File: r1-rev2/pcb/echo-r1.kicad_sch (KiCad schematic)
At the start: 82 parts, among them J2 TYPE-C-31-M-12, J3 TF-115, J6 PM254-1-06-W-8.5, J7 ILI9342C, J8 Conn_01x04, Q4 AO3401A, SW1 POWER, SW10 DPAD→, SW11 START, SW12 SELECT, SW13 VOL+, SW14 VOL-, SW2 HOLD, SW3 A, SW4 B, SW5 X, SW6 Y, SW7 DPAD↑, SW8 DPAD↓, SW9 DPAD←, U7 STM32H7R3Z8Jx, U8 W958D8NBYA5I, Y1 SC-32S32.768kHz20PPM12.5pF, Y2 XTM32024000JT00351001

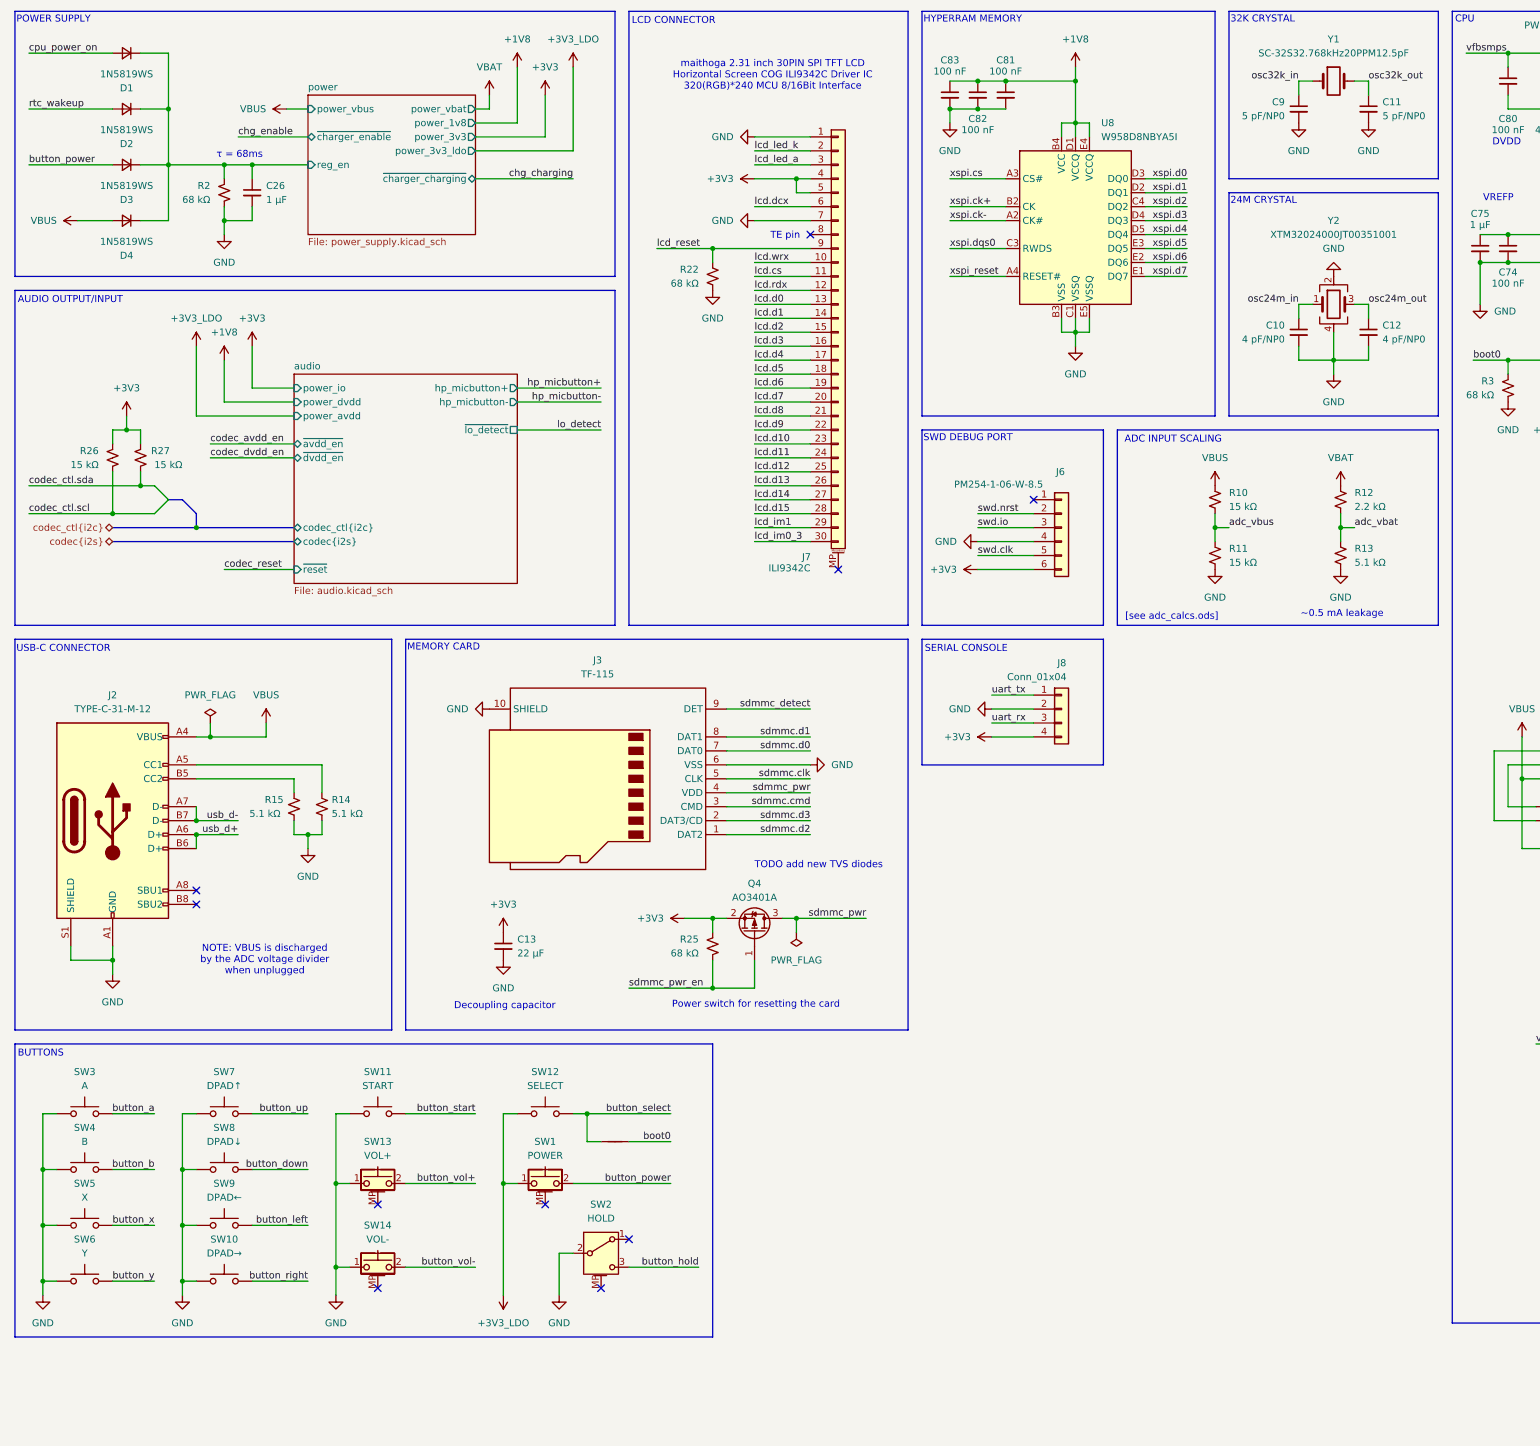
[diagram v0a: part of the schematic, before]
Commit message: R1-Rev2: add TVS diodes to external connectors
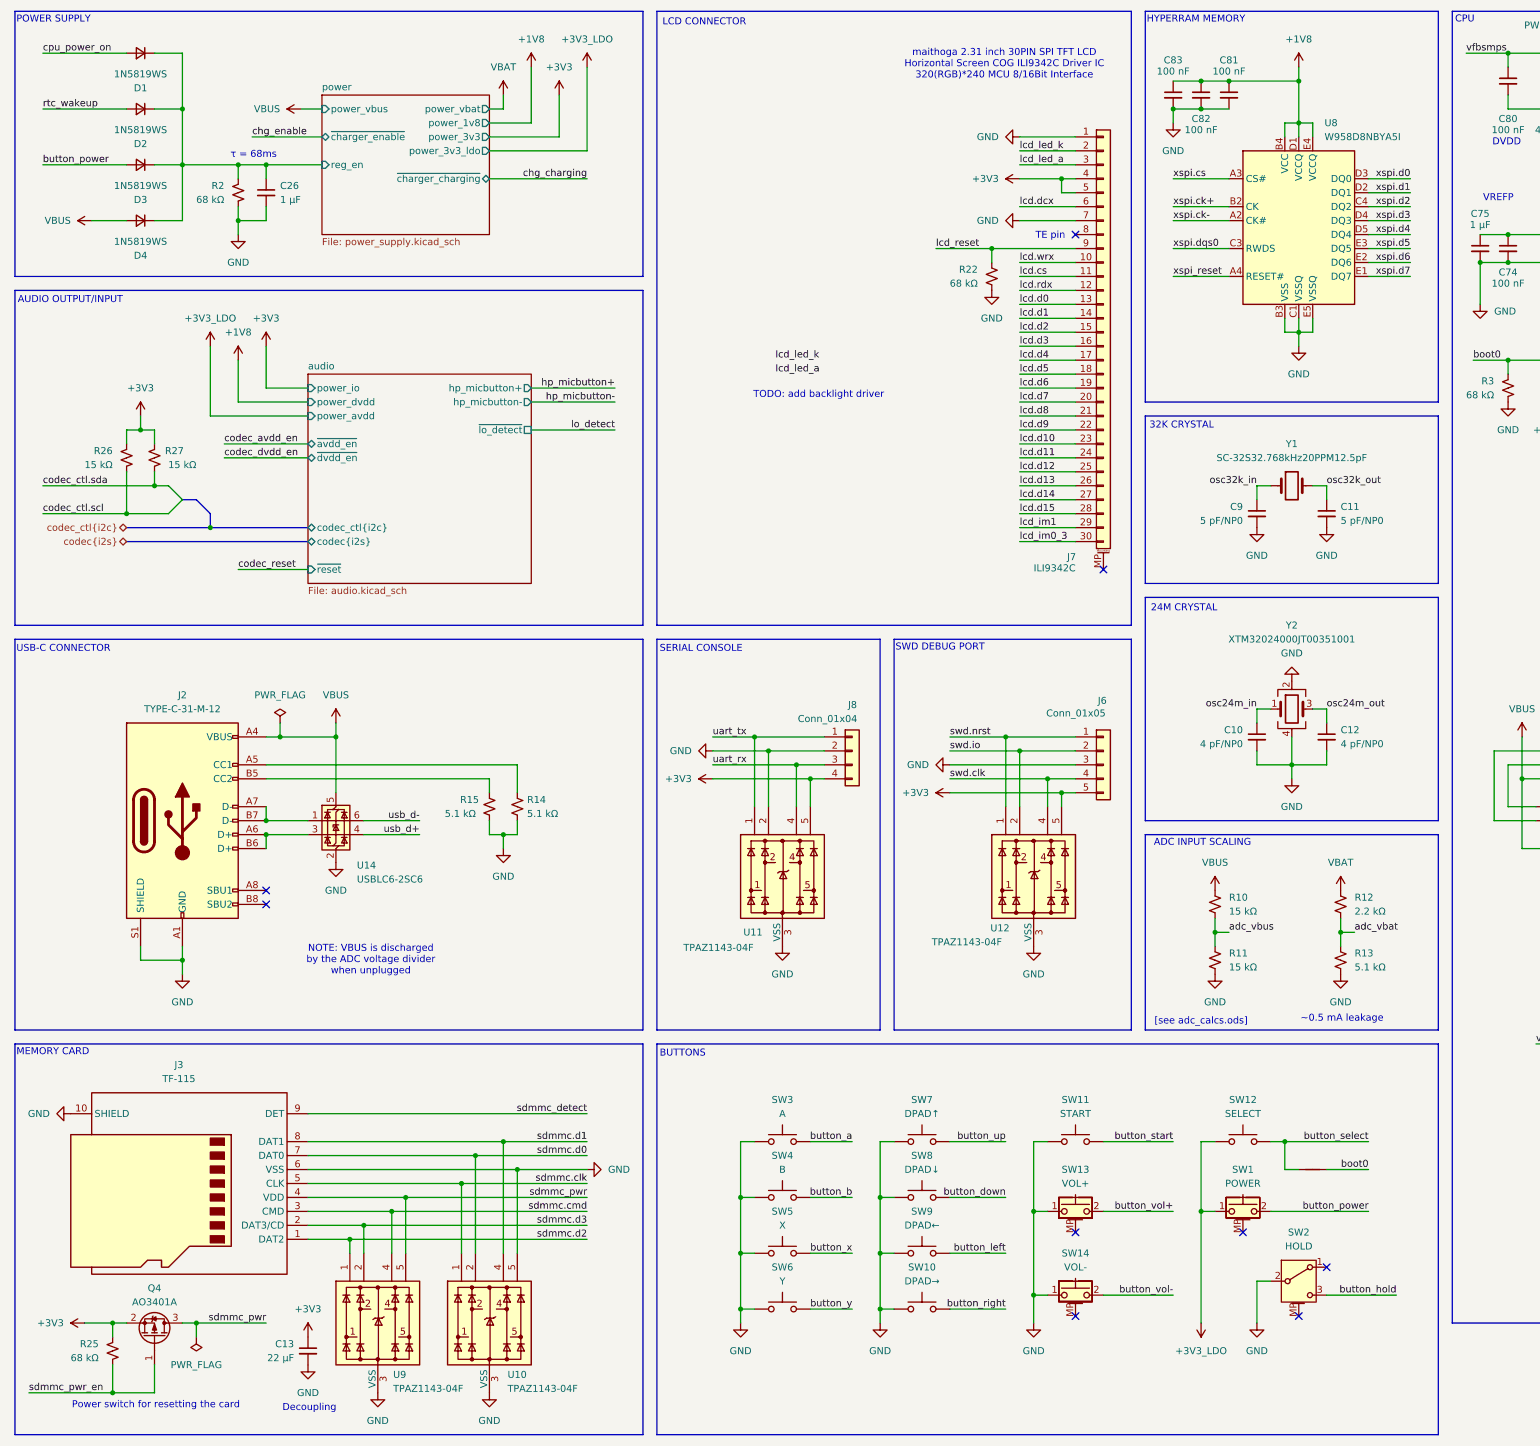
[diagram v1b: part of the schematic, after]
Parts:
- removed J6: PM254-1-06-W-8.5, Connector_PinSocket_2.54mm:PinSocket_1x06_P2.54mm_Horizontal, symbol Connector_Generic:Conn_01x06
- added J6: Conn_01x05, symbol Connector_Generic:Conn_01x05
- added U10, U11, U12, U9: TPAZ1143-04F, echoplayer:TECHPUBLIC_UDFN-10_1.0x2.5mm_P0.5mm, symbol echoplayer:TPAZ1143-04F
- added U14: USBLC6-2SC6, Package_TO_SOT_SMD:SOT-23-6, symbol Power_Protection:USBLC6-2SC6
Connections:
- net +3V3: now also J6.5 (Pin_5), U11.5, U12.5
- net GND: now also J6.3 (Pin_3), U10.10 (NC), U10.3 (VSS), U10.5, U10.6 (NC), U10.7 (NC), U10.8 (VSS), U10.9 (NC), U11.10 (NC), U11.2, U11.3 (VSS), U11.6 (NC), U11.7 (NC), U11.8 (VSS), U11.9 (NC), U12.10 (NC), U12.3 (VSS), U12.6 (NC), U12.7 (NC), U12.8 (VSS), U12.9 (NC), U14.2 (GND), U9.10 (NC), U9.3 (VSS), U9.6 (NC), U9.7 (NC), U9.8 (VSS), U9.9 (NC)
- net VBUS: now also U14.5 (VBUS)
- net sdmmc.clk: now also U10.1
- net sdmmc.cmd: now also U9.4
- net sdmmc.d0: now also U10.2
- net sdmmc.d1: now also U10.4
- net sdmmc.d2: now also U9.1
- net sdmmc.d3: now also U9.2
- net sdmmc_pwr: now also U9.5
- net swd.clk: now also J6.4 (Pin_4), U12.4
- net swd.io: now also J6.2 (Pin_2), U12.2
- net swd.nrst: now also J6.1 (Pin_1), U12.1
- net uart_rx: now also U11.4
- net uart_tx: now also U11.1
- net usb_d+: now also U14.4 (I/O2); no longer J2.A6 (D+), J2.B6 (D+)
- net usb_d-: now also U14.6 (I/O1); no longer J2.A7 (D-), J2.B7 (D-)
- new net: J2.A7 (D-), J2.B7 (D-), U14.1 (I/O1)
- new net: J2.A6 (D+), J2.B6 (D+), U14.3 (I/O2)
- no-connect marks 12 -> 11
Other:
- note added: "Decoupling"
- note added: "TODO: add backlight driver"
- note removed: "Decoupling capacitor"
- note removed: "TODO add new TVS diodes"
- moved on the sheet: C10, C11, C12, C13, C26, C81, C82, C83, C9, D1, D2, D3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

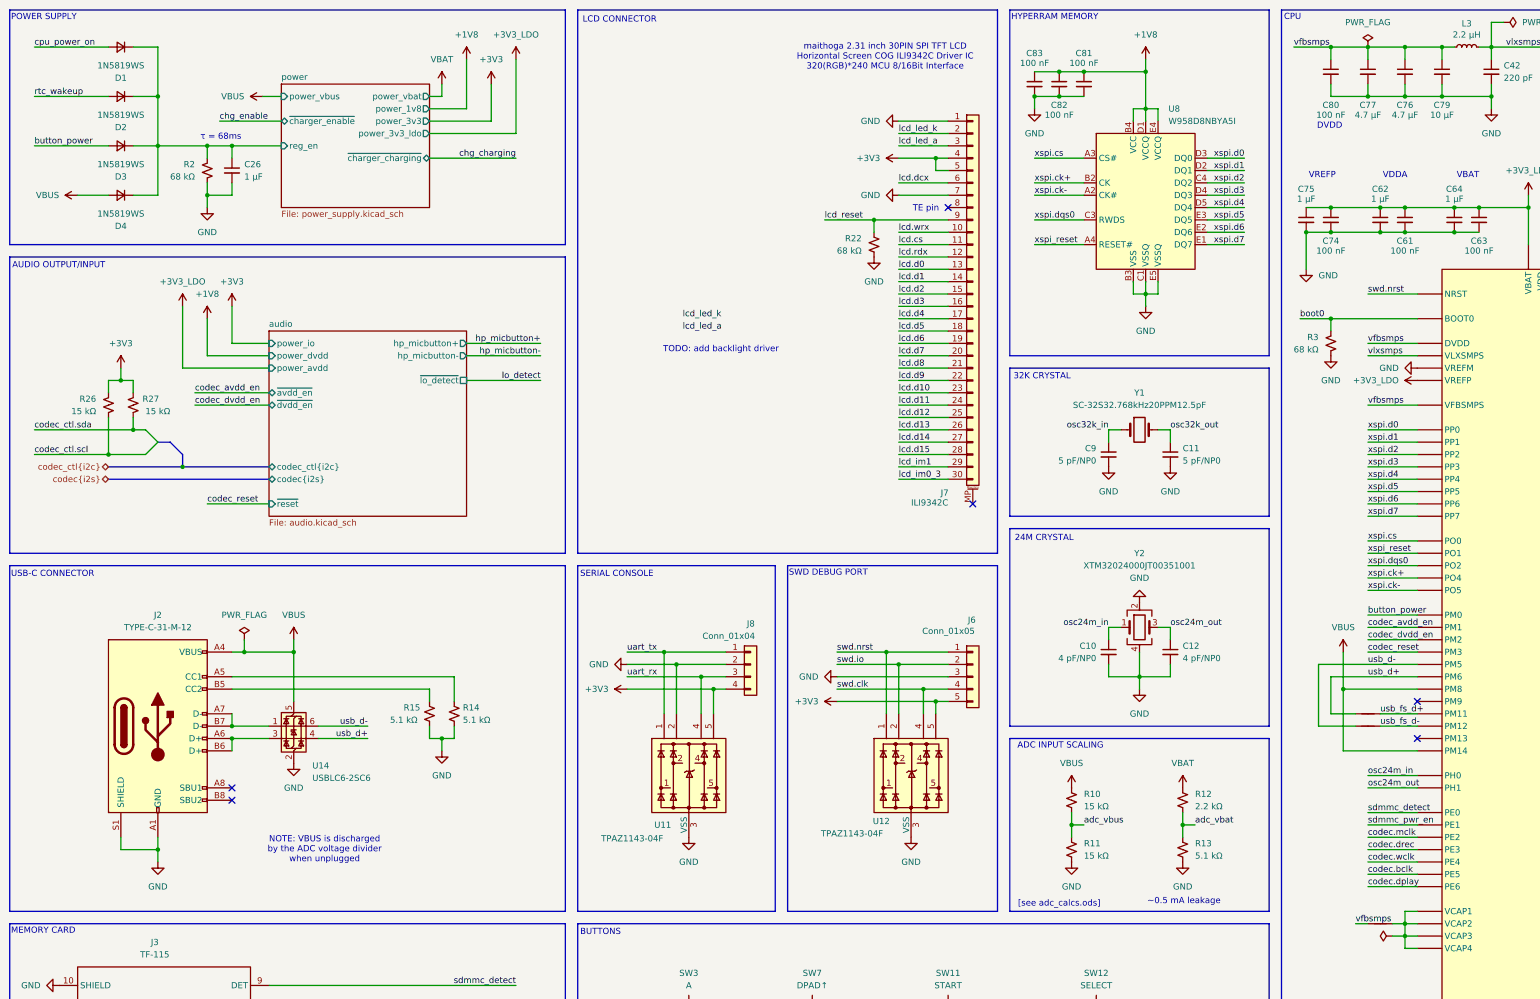
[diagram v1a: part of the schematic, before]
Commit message: R1-Rev2: add LCD backlight driver
The LEDs in the backlight will be in series since there are only
two pins, but it's not clear how many LEDs are there and without
that it's not possible to set the right current limit.
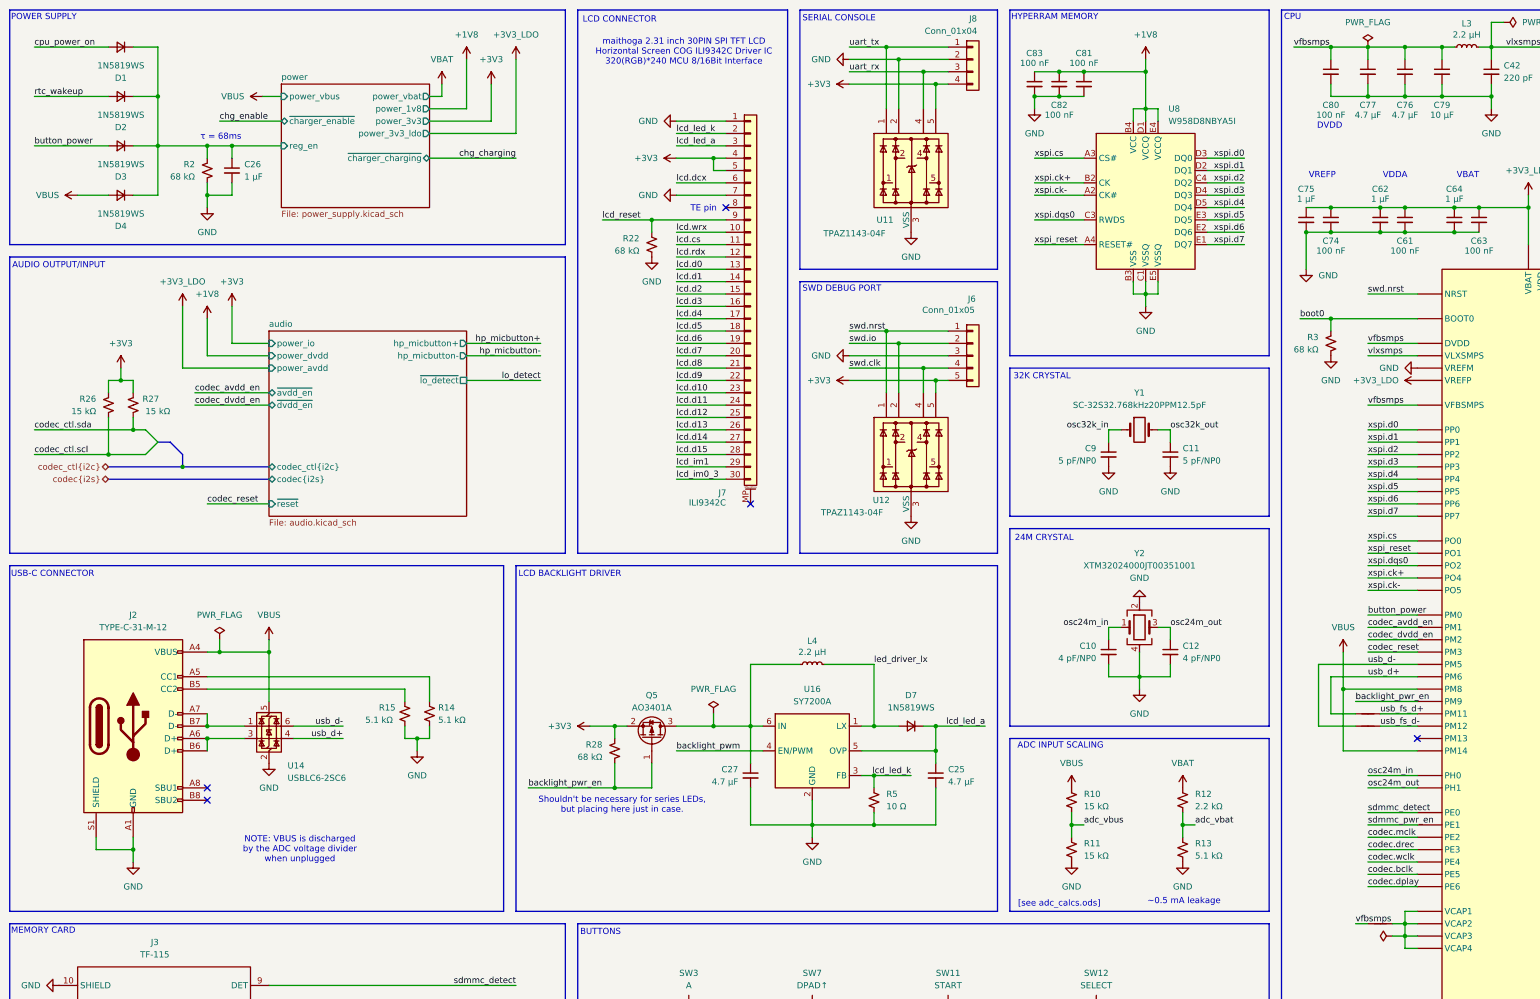
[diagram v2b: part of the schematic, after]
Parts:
- added C25, C27: 4.7 µF, Capacitor_SMD:C_0402_1005Metric, symbol Device:C_Small
- added D7: 1N5819WS, Diode_SMD:D_SOD-323, symbol Device:D_Small
- added L4: 2.2 µH, symbol Device:L_Small
- added Q5: AO3401A, Package_TO_SOT_SMD:SOT-23, symbol Device:Q_PMOS_GSD
- added R28: 68 kΩ, Resistor_SMD:R_0402_1005Metric, symbol Device:R_Small_US
- added R5: 10 Ω, Resistor_SMD:R_0402_1005Metric, symbol Device:R_Small_US
- added U16: SY7200A, Package_TO_SOT_SMD:SOT-23-6, symbol echoplayer:SY7200A
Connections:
- net +3V3: now also Q5.2 (S), R28.1
- net GND: now also C25.2, C27.2, R5.2, U16.2 (GND)
- net backlight_pwm: now also U16.4 (EN/PWM)
- net lcd_led_a: now also C25.1, D7.1 (K), U16.5 (OVP)
- net lcd_led_k: now also R5.1, U16.3 (FB)
- net backlight_pwr_en: now reaches U7.A8 (PM9)
- net backlight_pwr_en: now also Q5.1 (G), R28.2
- new net: C27.1, L4.1, Q5.3 (D), U16.6 (IN)
- new net led_driver_lx: D7.2 (A), L4.2, U16.1 (LX)
- no-connect marks 11 -> 10
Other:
- note added: "LCD BACKLIGHT DRIVER"
- note added: "Shouldn't be necessary for series LEDs, but placing here just in case."
- note removed: "TODO: add backlight driver"
- moved on the sheet: J2, J6, J7, J8, R14, R15, R22, U11, U12, U14
